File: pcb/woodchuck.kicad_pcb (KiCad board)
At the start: 2 copper layers, 18 parts, among them IC703 MS5611-01BA03, U1 Radiometrix_MTX2, U2 STM32F072CBT6

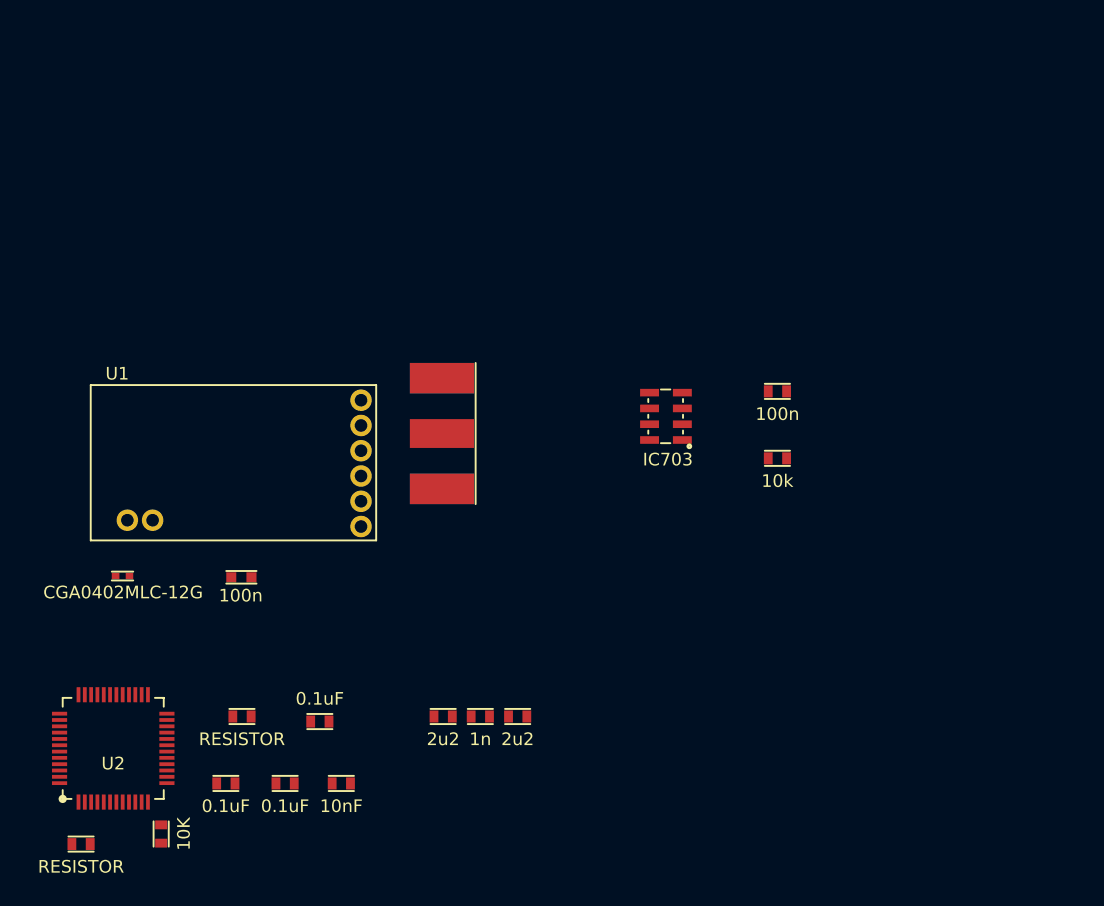
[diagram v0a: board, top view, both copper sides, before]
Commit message: Generated net list (only two footprints remaining), added a few footprints, started rough estimate of PCB size
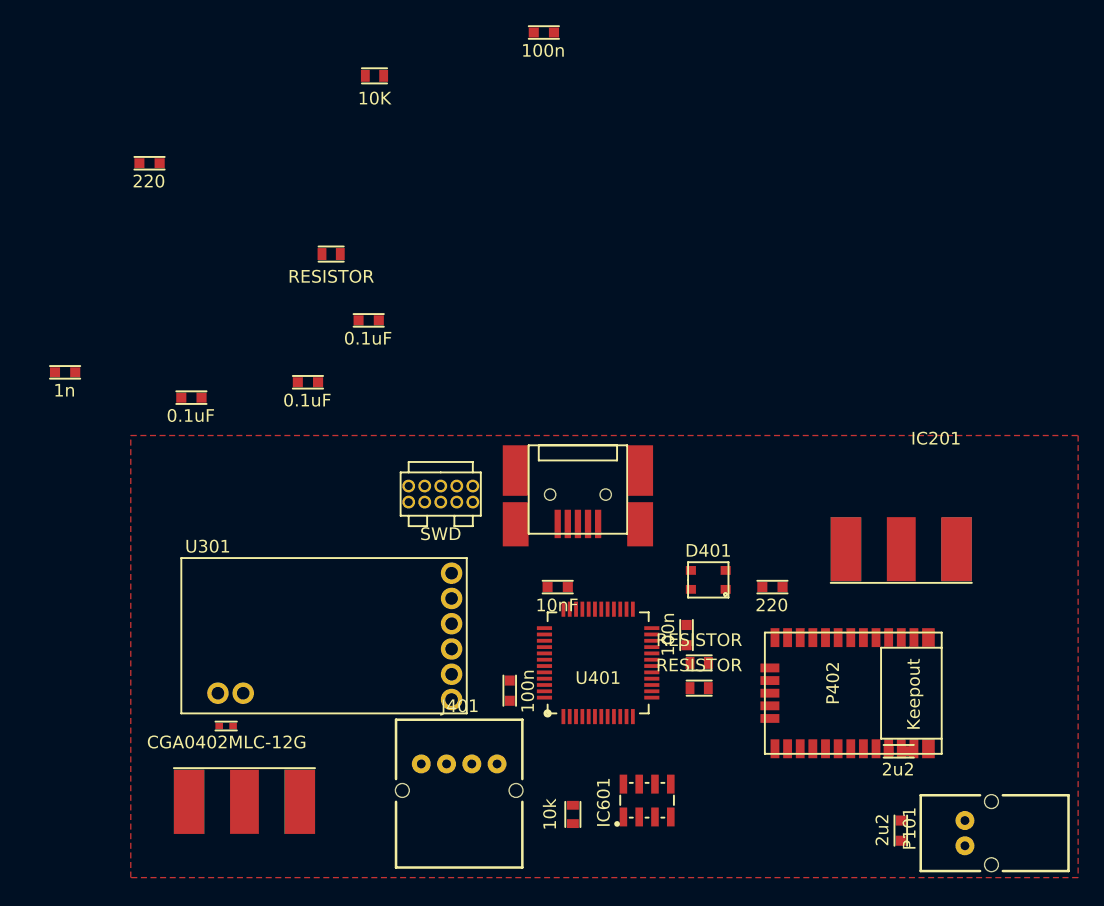
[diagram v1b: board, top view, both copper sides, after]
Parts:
- removed A1: SMA, Woodchuck:SMA-142-0701-801
- removed C1, C3: 2u2, Woodchuck:0603
- removed C2: 1n, Woodchuck:0603
- removed C4: 100n, Woodchuck:C0603
- removed C5: 10nF, Woodchuck:0603
- removed C6, C7, C8: 0.1uF, Woodchuck:0603
- removed C708: 100n, Woodchuck:0603
- removed D1: CGA0402MLC-12G, Woodchuck:R0402
- removed IC703: MS5611-01BA03, Woodchuck:MS5611-01BA
- removed R1: 10K, Woodchuck:0603
- removed R2, R3: RESISTOR, Woodchuck:0603
- removed R706: 10k, Woodchuck:0603
- removed U1: Radiometrix_MTX2, Woodchuck:MTX2
- removed U2: STM32F072CBT6, Woodchuck:LQFP48
- added A301: SMA, Woodchuck:SMA-142-0701-801, F.Cu at (159.0, 129.0)
- added C101: 2u2, Woodchuck:C0603, F.Cu at (211.0, 130.5)
- added C102: 1n, Woodchuck:C0603, F.Cu at (144.0, 95.0)
- added C103: 2u2, Woodchuck:C0603, F.Cu at (210.0, 125.0)
- added C201: 100n, Woodchuck:C0603, F.Cu at (181.9, 68.1)
- added C301: 100n, Woodchuck:C0603, F.Cu at (194.0, 115.0)
- added C401: 10nF, Woodchuck:C0603, F.Cu at (183.0, 112.0)
- added C402: 0.1uF, Woodchuck:C0603, F.Cu at (154.0, 97.0)
- added C403: 0.1uF, Woodchuck:C0603, F.Cu at (163.2, 95.8)
- added C404: 0.1uF, Woodchuck:C0603, F.Cu at (168.0, 90.9)
- added C601: 100n, Woodchuck:C0603, F.Cu at (180.0, 121.0)
- added D301: CGA0402MLC-12G, Woodchuck:R0402, F.Cu at (157.0, 123.0)
- added D401: LED_RCBG, Woodchuck:CREE_RGB_LED, F.Cu at (195.7, 111.4)
- added IC201: u-blox_CAM-M8Q, Woodchuck:UBLOX_CAM_M8Q, F.Cu at (201.0, 116.0)
- added IC601: MS5611-01BA03, Woodchuck:MS5611-01BA, F.Cu at (189.0, 130.0)
- added J401: JSTA-4, Woodchuck:S04B-PASK-2, F.Cu at (179.0, 126.0)
- added P101: CONN_01X02, Woodchuck:S02B-PASK-2, F.Cu at (216.0, 130.5)
- added P201: SMA, Woodchuck:SMA-142-0701-801, F.Cu at (211.0, 109.0)
- added P401: SWD, Woodchuck:FTSH-105-01-F-D-K, F.Cu at (172.0, 104.0)
- added P402: USB_OTG, Woodchuck:MOLEX_67503_1020_MINI_USB, F.Cu at (187.0, 107.0)
- added R201: 220, Woodchuck:C0603, F.Cu at (150.7, 78.4)
- added R202: 220, Woodchuck:C0603, F.Cu at (200.0, 112.0)
- added R401: RESISTOR, Woodchuck:0603, F.Cu at (195.0, 120.0)
- added R402: RESISTOR, Woodchuck:0603, F.Cu at (165.9, 85.6)
- added R403: RESISTOR, Woodchuck:0603, F.Cu at (195.0, 118.0)
- added R404: 10K, Woodchuck:0603, F.Cu at (169.3, 71.5)
- added R601: 10k, Woodchuck:0603, F.Cu at (185.0, 130.0)
- added U301: Radiometrix_MTX2, Woodchuck:MTX2, F.Cu at (154.0, 122.0)
- added U401: STM32F072CBT6, Woodchuck:LQFP48, F.Cu at (187.0, 118.0)
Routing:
- added copper zone on F.Cu, net (none)

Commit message: Begin placing PCB components
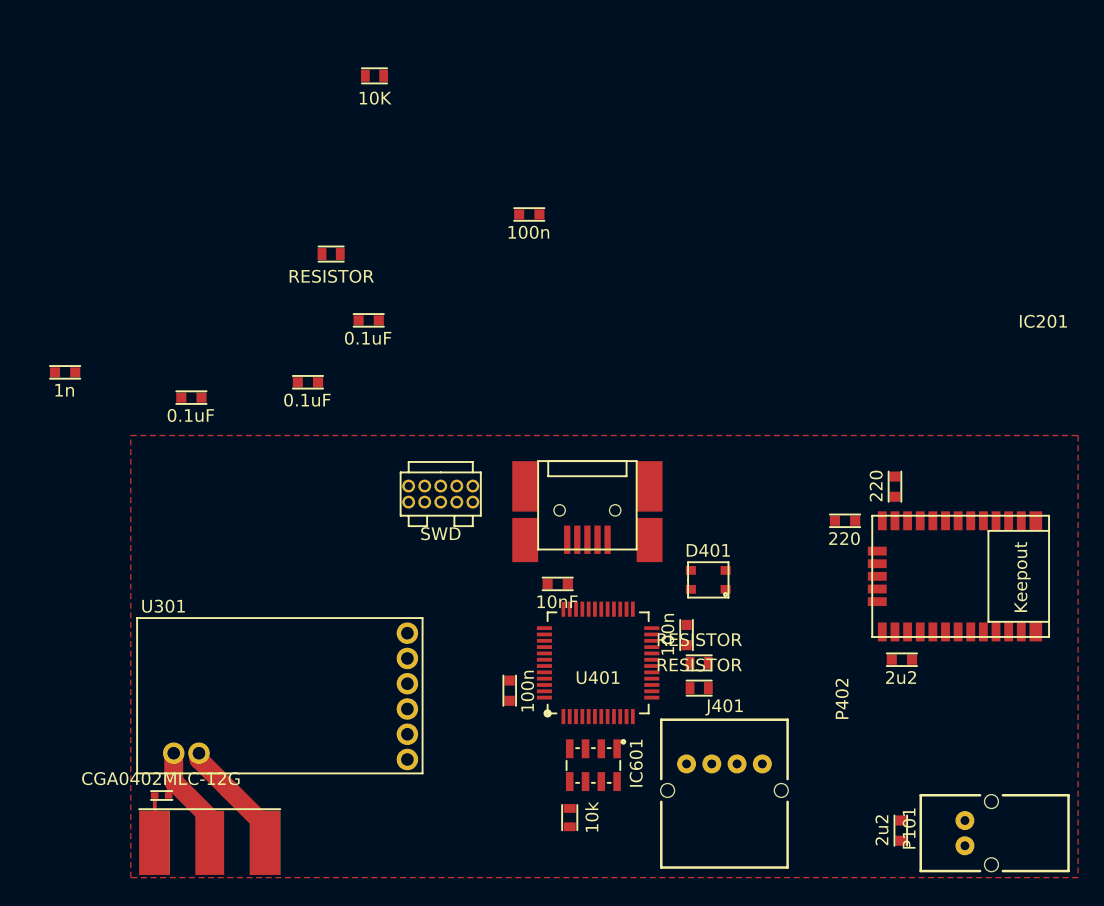
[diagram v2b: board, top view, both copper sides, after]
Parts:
- removed P201: SMA, Woodchuck:SMA-142-0701-801
- moved R201 64.8 mm to (210.5, 103.2), turned to 270 degrees
- moved J401 21.0 mm to (200.0, 126.0)
- moved C201 14.5 mm to (180.8, 82.5)
- moved IC201 12.6 mm to (209.5, 106.8)
- moved R202 7.79 mm to (205.8, 106.8)
- moved C103 7.25 mm to (210.2, 117.8)
- moved D301 6.80 mm to (153.0, 128.5), turned to 180 degrees
- moved U301 5.90 mm to (150.5, 126.8)
- moved IC601 5.02 mm to (188.5, 125.0), turned to 270 degrees
- moved A301 4.26 mm to (156.2, 132.2)
- moved P402 1.46 mm to (187.8, 108.2)
- moved R601 0.35 mm to (184.8, 130.2), turned to 90 degrees
- moved C401 0.25 mm to (183.0, 111.8)
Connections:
- IC201 pad 17: Net-(IC201-Pad17) -> Net-(IC201-Pad16)
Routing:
- net GND: track 0.00 -> 10.6 mm
- net Net-(A301-Pad1): track 0.00 -> 9.55 mm

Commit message: Fixed the planes
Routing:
- added copper zone on B.Cu, net GND
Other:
- board outline added: 75 x 35 mm
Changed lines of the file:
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@@
-(kicad_pcb (version 4) (host pcbnew 4.0.0-rc1-stable)
+(kicad_pcb (version 4) (host pcbnew 4.0.1-4.201602090852+6195~38~ubuntu14.04.1-stable)
   (general
     (links 101)
-    (no_connects 84)
-    (area 0 0 0 0)
+    (no_connects 79)
+    (area 142.496429 69 225.075001 137.035)
     (thickness 1.6)
-    (drawings 0)
+    (drawings 4)
     (tracks 11)
     (zones 0)
@@
   )
   (setup
-    (last_trace_width 0.3)
+    (last_trace_width 0.25)
     (user_trace_width 0.3)
     (user_trace_width 1)
@@
       (net 53 "Net-(D401-Pad3)"))
   )
+  (gr_line (start 150 135) (end 150 100) (angle 90) (layer Edge.Cuts) (width 0.15))
+  (gr_line (start 225 135) (end 150 135) (angle 90) (layer Edge.Cuts) (width 0.15))
+  (gr_line (start 225 100) (end 225 135) (angle 90) (layer Edge.Cuts) (width 0.15))
+  (gr_line (start 150 100) (end 225 100) (angle 90) (layer Edge.Cuts) (width 0.15))
   (segment (start 151.9 128.5) (end 151.9 132.2185) (width 0.3) (layer F.Cu) (net 1))
   (segment (start 151.9 132.2185) (end 151.8685 132.25) (width 0.3) (layer F.Cu) (net 1))
@@
     (connect_pads (clearance 0.508))
     (min_thickness 0.254)
-    (fill (arc_segments 16) (thermal_gap 0.508) (thermal_bridge_width 0.508))
+    (fill yes (arc_segments 16) (thermal_gap 0.508) (thermal_bridge_width 0.508))
     (polygon
       (pts
+        (xy 225 135) (xy 150 135) (xy 150 100) (xy 225 100) (xy 225 135)
+      )
+    )
+  )
+  (zone (net 1) (net_name GND) (layer B.Cu) (hatch edge 0.508)
+    (connect_pads (clearance 0.508))
+    (min_thickness 0.254)
+    (fill yes (arc_segments 16) (thermal_gap 0.508) (thermal_bridge_width 0.508))
+    (polygon
+      (pts
